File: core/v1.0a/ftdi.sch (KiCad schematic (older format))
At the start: 33 parts, among them J1 Conn, P1 pkl_USB_OTG, P2 UP, P3 UP, P4 UP, P5 UP, U1 93C46B-SOT-23-6, U2 FT232H, X1 12MHz

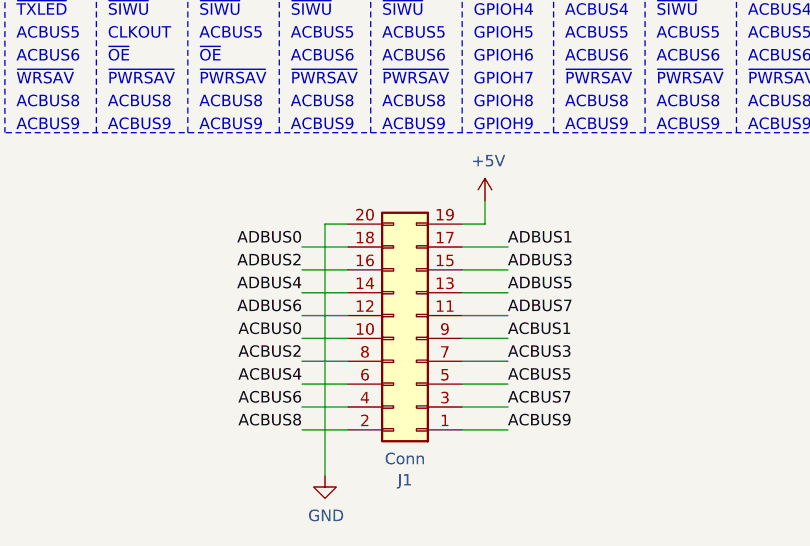
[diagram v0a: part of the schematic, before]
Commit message: Bumped the ftdi adapter to V1.0a. + minor improvements.
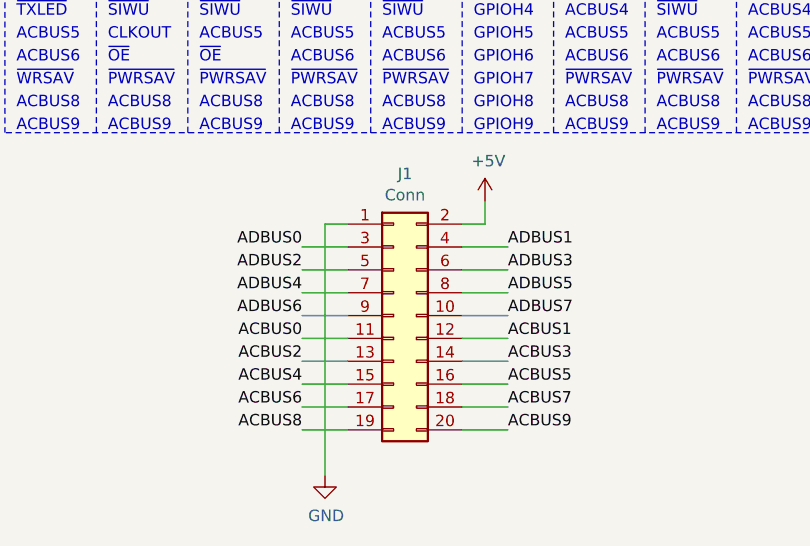
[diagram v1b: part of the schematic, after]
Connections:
- net +5V: now also J1.2 (Pin_2); no longer J1.19 (Pin_19)
- net ACBUS0: now also J1.11 (Pin_11); no longer J1.10 (Pin_10)
- net ACBUS1: now also J1.12 (Pin_12); no longer J1.9 (Pin_9)
- net ACBUS2: now also J1.13 (Pin_13); no longer J1.8 (Pin_8)
- net ACBUS3: now also J1.14 (Pin_14); no longer J1.7 (Pin_7)
- net ACBUS4: now also J1.15 (Pin_15); no longer J1.6 (Pin_6)
- net ACBUS5: now also J1.16 (Pin_16); no longer J1.5 (Pin_5)
- net ACBUS6: now also J1.17 (Pin_17); no longer J1.4 (Pin_4)
- net ACBUS7: now also J1.18 (Pin_18); no longer J1.3 (Pin_3)
- net ACBUS8: now also J1.19 (Pin_19); no longer J1.2 (Pin_2)
- net ACBUS9: now also J1.20 (Pin_20); no longer J1.1 (Pin_1)
- net ADBUS0: now also J1.3 (Pin_3); no longer J1.18 (Pin_18)
- net ADBUS1: now also J1.4 (Pin_4); no longer J1.17 (Pin_17)
- net ADBUS2: now also J1.5 (Pin_5); no longer J1.16 (Pin_16)
- net ADBUS3: now also J1.6 (Pin_6); no longer J1.15 (Pin_15)
- net ADBUS4: now also J1.7 (Pin_7); no longer J1.14 (Pin_14)
- net ADBUS5: now also J1.8 (Pin_8); no longer J1.13 (Pin_13)
- net ADBUS6: now also J1.9 (Pin_9); no longer J1.12 (Pin_12)
- net ADBUS7: now also J1.10 (Pin_10); no longer J1.11 (Pin_11)
- net GND: now also J1.1 (Pin_1); no longer J1.20 (Pin_20)
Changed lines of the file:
@@
 Title "ftdi breakout"
 Date ""
-Rev "V0.2a"
+Rev "V1.0a"
 Comp "1BitSquared"
 Comment1 "2018 (C) 1BitSquared <info@1bitsquared.com>"
@@
 L Connector_Generic:Conn_02x10_Odd_Even J1
 U 1 1 5BD3E874
-P 8400 5400
-F 0 "J1" H 8450 6020 50  0000 C CNN
-F 1 "Conn" H 8450 5927 50  0000 C CNN
-F 2 "pkl_samtec:FTSH-EDGE-20pin" H 8400 5400 50  0001 C CNN
-F 3 "~" H 8400 5400 50  0001 C CNN
-F 4 "conn-th-01in-2-10-hdr-ra" H 100 0   50  0001 C CNN "Key"
-F 5 "ANY" H 8400 5400 50  0001 C CNN "Source"
-	1    8400 5400
-	-1   0    0    1
+P 8300 5300
+F 0 "J1" H 8350 5920 50  0000 C CNN
+F 1 "Conn" H 8350 5827 50  0000 C CNN
+F 2 "pkl_samtec:FTSH-EDGE-20pin" H 8300 5300 50  0001 C CNN
+F 3 "~" H 8300 5300 50  0001 C CNN
+F 4 "conn-th-01in-2-10-hdr-ra" H 0   -100 50  0001 C CNN "Key"
+F 5 "ANY" H 8300 5300 50  0001 C CNN "Source"
+	1    8300 5300
+	1    0    0    -1
 $EndComp
 Text Label 7900 5000 2    50   ~ 0

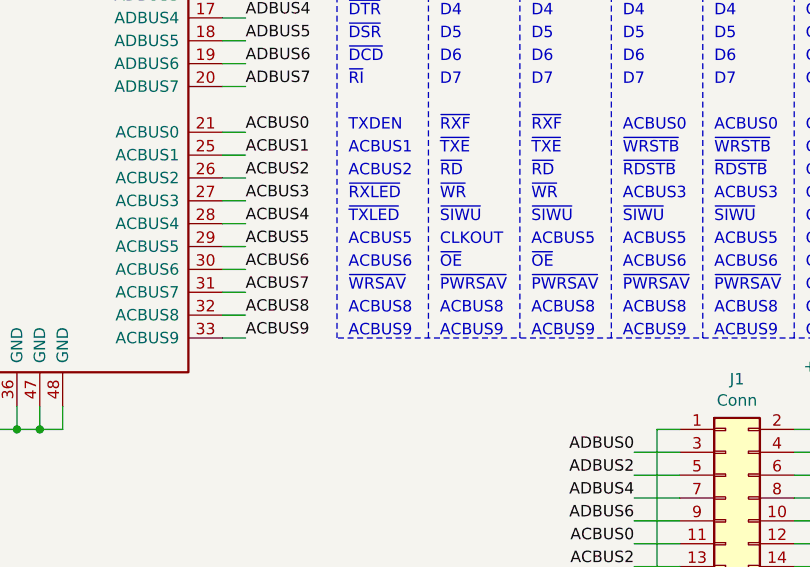
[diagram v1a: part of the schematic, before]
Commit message: A bunch of minor fixes.
* PWRSAV instead of WRSAV in signal table.
* 0.05 solder stop opening instead of 0.2
* Better copper fill parameters.
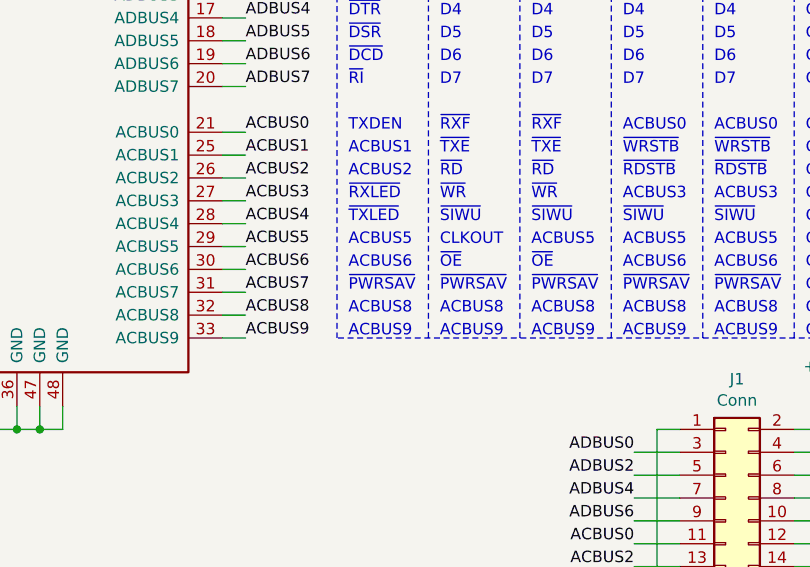
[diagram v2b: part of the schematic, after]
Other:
- note removed: "~WRSAV"
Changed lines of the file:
@@
 ACBUS6
 Text Notes 6650 4300 0    50   ~ 0
-~WRSAV
+~PWRSAV
 Text Notes 6650 4400 0    50   ~ 0
 ACBUS8
